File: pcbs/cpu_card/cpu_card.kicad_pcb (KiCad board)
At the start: 4 copper layers, 100 x 100 mm, 12 parts, among them J1 Conn1, J2 osc_header, U1 74LS161, Y1 ECS-2100AX-100

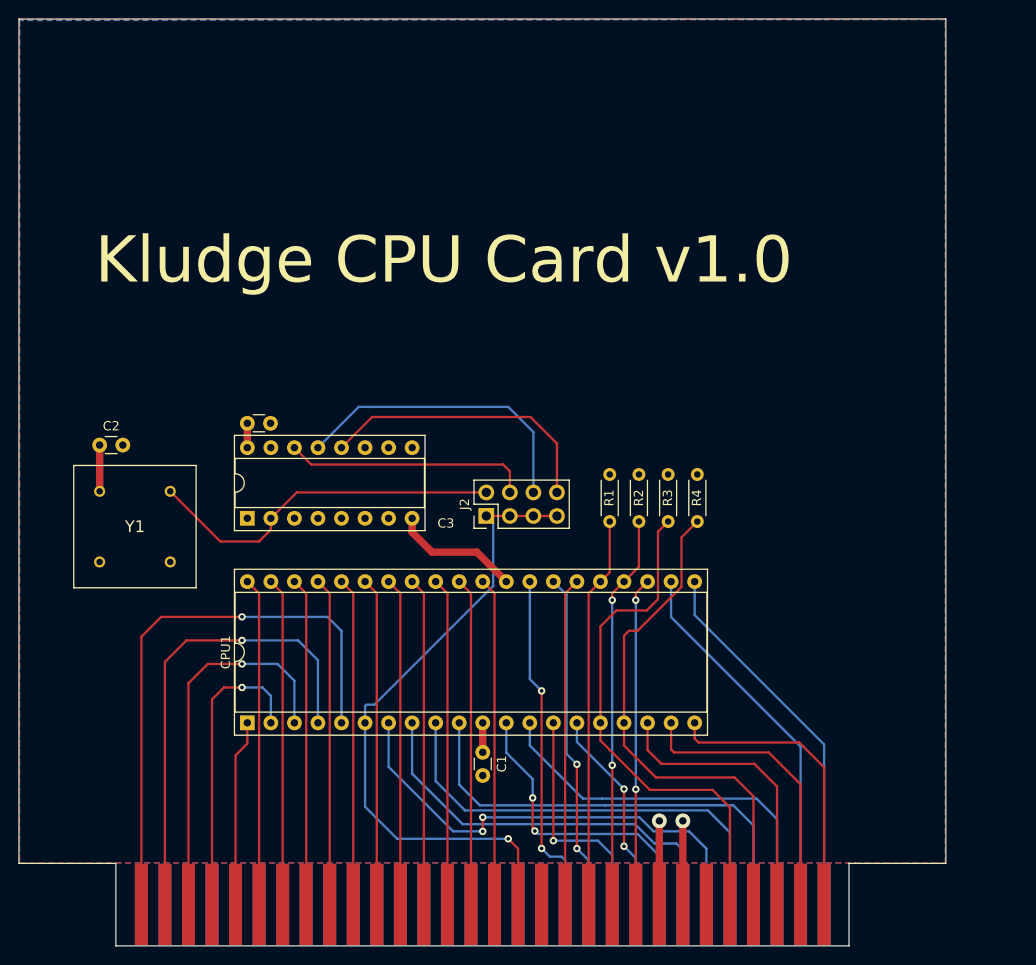
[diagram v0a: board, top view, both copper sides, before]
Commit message: changed signal traces from 0.25mm to 0.3mm and moved a few traces arround to accommodate the new size
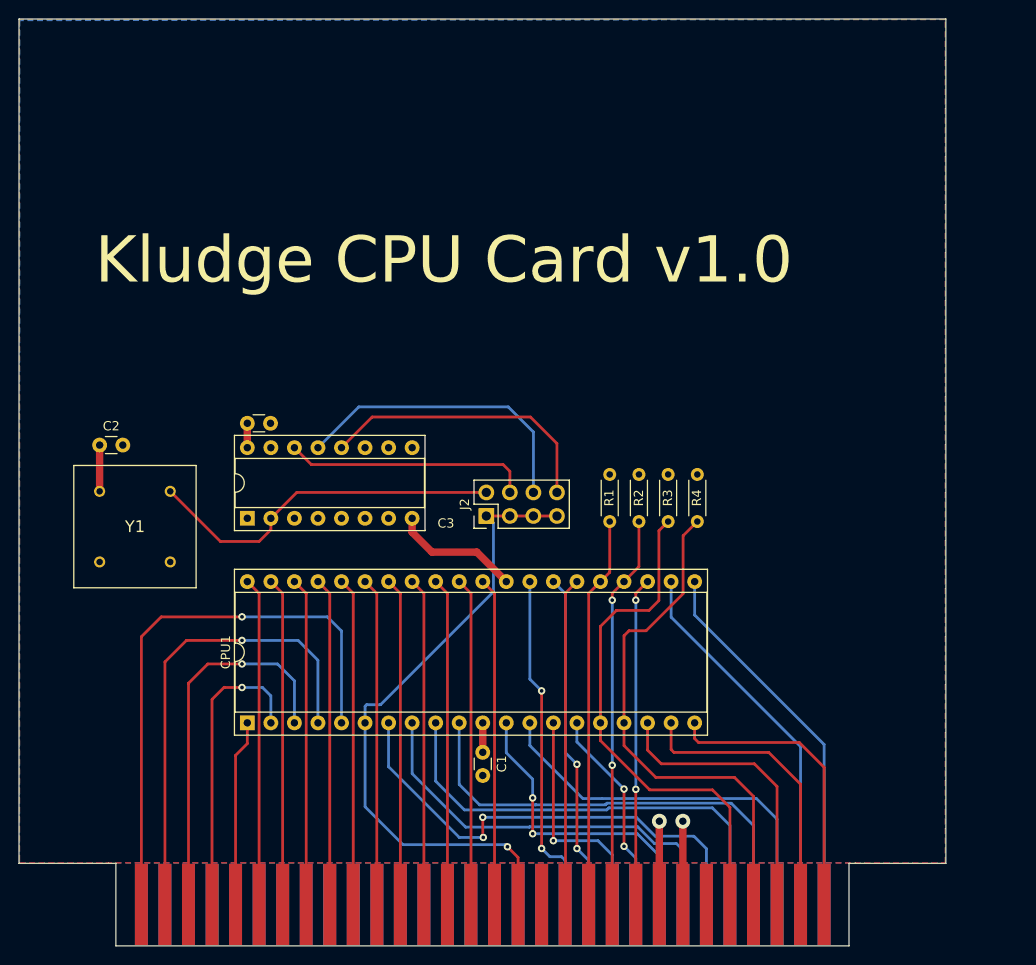
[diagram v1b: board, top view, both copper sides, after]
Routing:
- net /D4: track 50.9 -> 51.9 mm
- net /D5: track 48.1 -> 48.7 mm
- net NMI: track 55.9 -> 56.4 mm

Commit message: Changed the bus hardware to 2.54mm header and cleaned up the CPU card PCB layout
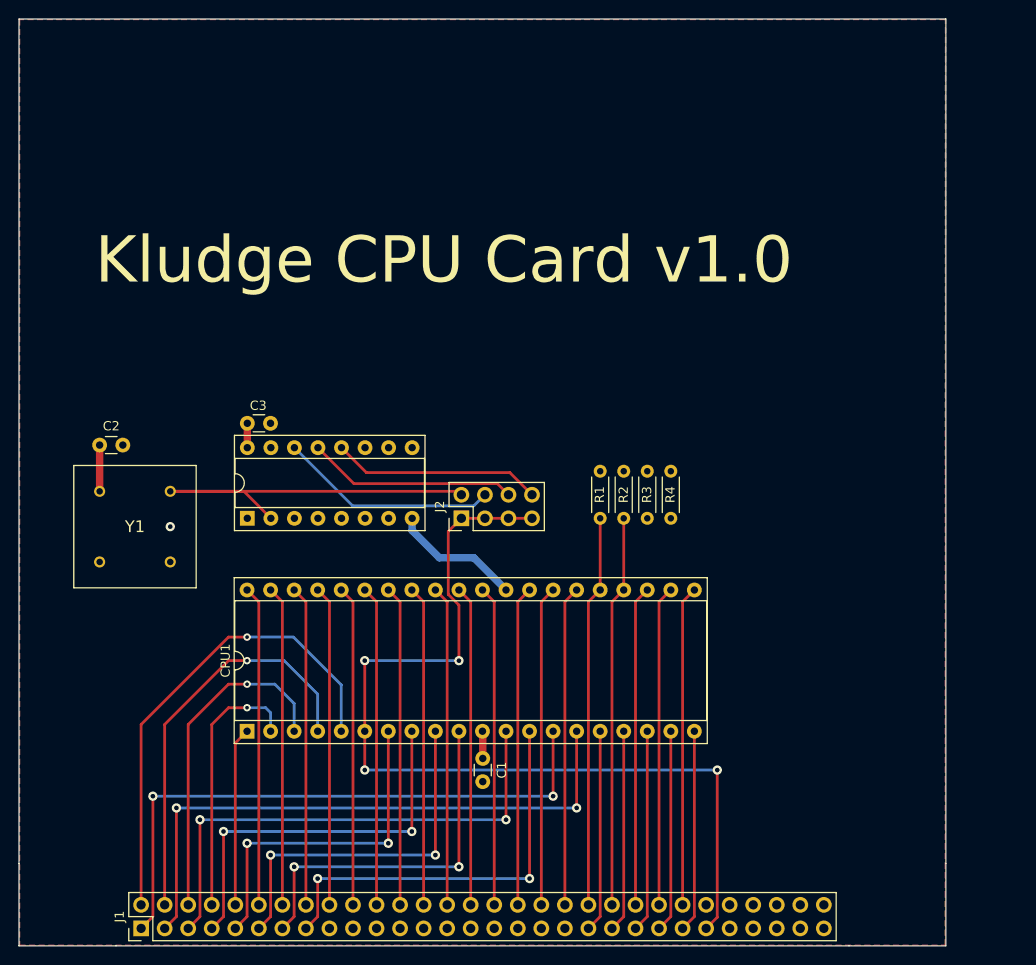
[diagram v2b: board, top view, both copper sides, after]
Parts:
- J1: footprint Z80 Parts:2x30-edge-connector -> Connector_PinHeader_2.54mm:PinHeader_2x30_P2.54mm_Vertical
- R1, R2, R3, R4: value 10K -> 3.3K
- moved J1 39.7 mm to (113.2, 148.1), turned to 90 degrees
- moved R4 2.88 mm to (170.3, 103.9)
- moved J2 2.70 mm to (147.7, 103.9)
- moved R3 2.28 mm to (167.8, 103.9)
- moved R2 1.68 mm to (165.2, 103.9)
- moved R1 1.09 mm to (162.7, 103.9)
- moved CPU1 0.91 mm to (124.6, 126.8)
- moved C1 0.66 mm to (150.0, 129.8)
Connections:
- J1 pad 1: /A15 -> /D0
- J1 pad 10: unconnected-(J1-Pin_10-Pad10) -> /A11
- J1 pad 11: /A10 -> /D5
- J1 pad 12: unconnected-(J1-Pin_12-Pad12) -> /A10
- J1 pad 13: /A9 -> /D6
- J1 pad 14: unconnected-(J1-Pin_14-Pad14) -> /A9
- J1 pad 15: /A8 -> /D7
- J1 pad 16: unconnected-(J1-Pin_16-Pad16) -> /A8
- J1 pad 17: /A7 -> unconnected-(J1-Pin_17-Pad17)
- J1 pad 18: unconnected-(J1-Pin_18-Pad18) -> /A7
- J1 pad 19: /A6 -> unconnected-(J1-Pin_19-Pad19)
- J1 pad 2: unconnected-(J1-Pin_2-Pad2) -> /A15
- J1 pad 20: unconnected-(J1-Pin_20-Pad20) -> /A6
- J1 pad 21: /A5 -> unconnected-(J1-Pin_21-Pad21)
- J1 pad 22: unconnected-(J1-Pin_22-Pad22) -> /A5
- J1 pad 23: /A4 -> unconnected-(J1-Pin_23-Pad23)
- J1 pad 24: unconnected-(J1-Pin_24-Pad24) -> /A4
- J1 pad 25: /A3 -> unconnected-(J1-Pin_25-Pad25)
- J1 pad 26: unconnected-(J1-Pin_26-Pad26) -> /A3
- J1 pad 27: /A2 -> unconnected-(J1-Pin_27-Pad27)
- J1 pad 28: unconnected-(J1-Pin_28-Pad28) -> /A2
- J1 pad 29: /A1 -> unconnected-(J1-Pin_29-Pad29)
- J1 pad 3: /A14 -> /D1
- J1 pad 30: unconnected-(J1-Pin_30-Pad30) -> /A1
- J1 pad 31: /A0 -> unconnected-(J1-Pin_31-Pad31)
- J1 pad 32: unconnected-(J1-Pin_32-Pad32) -> /A0
- J1 pad 33: SYSCLK -> GND
- J1 pad 34: unconnected-(J1-Pin_34-Pad34) -> RFSH
- J1 pad 35: unconnected-(J1-Pin_35-Pad35) -> VCC
- J1 pad 36: unconnected-(J1-Pin_36-Pad36) -> M1
- J1 pad 37: RESET -> RESET(H)
- J1 pad 38: RFSH -> RESET
- J1 pad 39: BUSRQ -> INT
- J1 pad 4: unconnected-(J1-Pin_4-Pad4) -> /A14
- J1 pad 40: M1 -> BUSRQ
- J1 pad 41: WAIT -> NMI
- J1 pad 42: /D0 -> WAIT
- J1 pad 43: BUSAK -> HALT
- J1 pad 44: /D1 -> BUSAK
- J1 pad 45: GND -> MREQ
- J1 pad 46: /D2 -> WR
- J1 pad 47: VCC -> IOREQ
- J1 pad 48: /D3 -> RD
- J1 pad 49: unconnected-(J1-Pin_49-Pad49) -> SYSCLK
- J1 pad 5: /A13 -> /D2
- J1 pad 50: /D4 -> unconnected-(J1-Pin_50-Pad50)
- J1 pad 51: INT -> unconnected-(J1-Pin_51-Pad51)
- J1 pad 52: /D5 -> unconnected-(J1-Pin_52-Pad52)
- J1 pad 53: NMI -> unconnected-(J1-Pin_53-Pad53)
- J1 pad 54: /D6 -> unconnected-(J1-Pin_54-Pad54)
- J1 pad 55: HALT -> unconnected-(J1-Pin_55-Pad55)
- J1 pad 56: /D7 -> unconnected-(J1-Pin_56-Pad56)
- J1 pad 57: MREQ -> unconnected-(J1-Pin_57-Pad57)
- J1 pad 58: WR -> unconnected-(J1-Pin_58-Pad58)
- J1 pad 59: IOREQ -> unconnected-(J1-Pin_59-Pad59)
- J1 pad 6: unconnected-(J1-Pin_6-Pad6) -> /A13
- J1 pad 60: RD -> unconnected-(J1-Pin_60-Pad60)
- J1 pad 7: /A12 -> /D3
- J1 pad 8: unconnected-(J1-Pin_8-Pad8) -> /A12
- J1 pad 9: /A11 -> /D4
- U1 pad 3: unconnected-(U1-D0-Pad3) -> GND
- U1 pad 4: unconnected-(U1-D1-Pad4) -> GND
- U1 pad 5: unconnected-(U1-D2-Pad5) -> GND
- U1 pad 6: unconnected-(U1-D3-Pad6) -> GND
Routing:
- net /D1: track 22.2 -> 65.0 mm
- net /D0: track 25.1 -> 65.0 mm, vias 1 -> 2
- net NMI: track 56.4 -> 21.8 mm
- net INT: track 56.2 -> 21.8 mm
- net SYSCLK: track 69.8 -> 101.6 mm, vias 1 -> 4
- net /D2: track 33.1 -> 54.8 mm
- net /D4: track 51.9 -> 37.0 mm
- net /1/4: track 32.7 -> 22.7 mm
- net IOREQ: track 31.8 -> 21.8 mm
- net /A15: track 61.9 -> 52.1 mm
- net MREQ: track 31.4 -> 21.8 mm
- net HALT: track 31.3 -> 21.8 mm
- net /D6: track 48.9 -> 39.6 mm, vias 0 -> 2
- net VCC: track 19.8 -> 10.6 mm, vias 1 -> 0
- net /D5: track 48.7 -> 39.6 mm, vias 0 -> 2
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- added copper zone on In1.Cu, net GND
- added copper zone on In2.Cu, net VCC
- removed copper zone on In2.Cu, net GND
- removed copper zone on In1.Cu, net VCC
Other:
- outline, holes or cut-outs redrawn

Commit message: Changed CPU board to nominal 20MHz with the option to adjust using the 2x5 header.
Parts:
- J2: footprint Connector_PinHeader_2.54mm:PinHeader_2x04_P2.54mm_Vertical -> Connector_PinHeader_2.54mm:PinHeader_2x05_P2.54mm_Vertical
- Y1: value ECS-2100AX-100 -> ECS-2100AX-200; footprint Z80 Parts:ECS-2100AX-100 -> Z80 Parts:ECS-2100AX-200
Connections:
- net /1/2 renamed /10 MHz
- net /1/4 renamed /5 MHz
- net /1/8 renamed /2.5 MHz
- U1 pad 11: unconnected-(U1-Q3-Pad11) -> /1.25 MHz
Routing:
- net NMI: track 21.8 -> 46.9 mm
- net INT: track 21.8 -> 46.9 mm
- net /1.25 MHz: track 0.00 -> 22.7 mm
- net SYSCLK: track 101.6 -> 104.2 mm

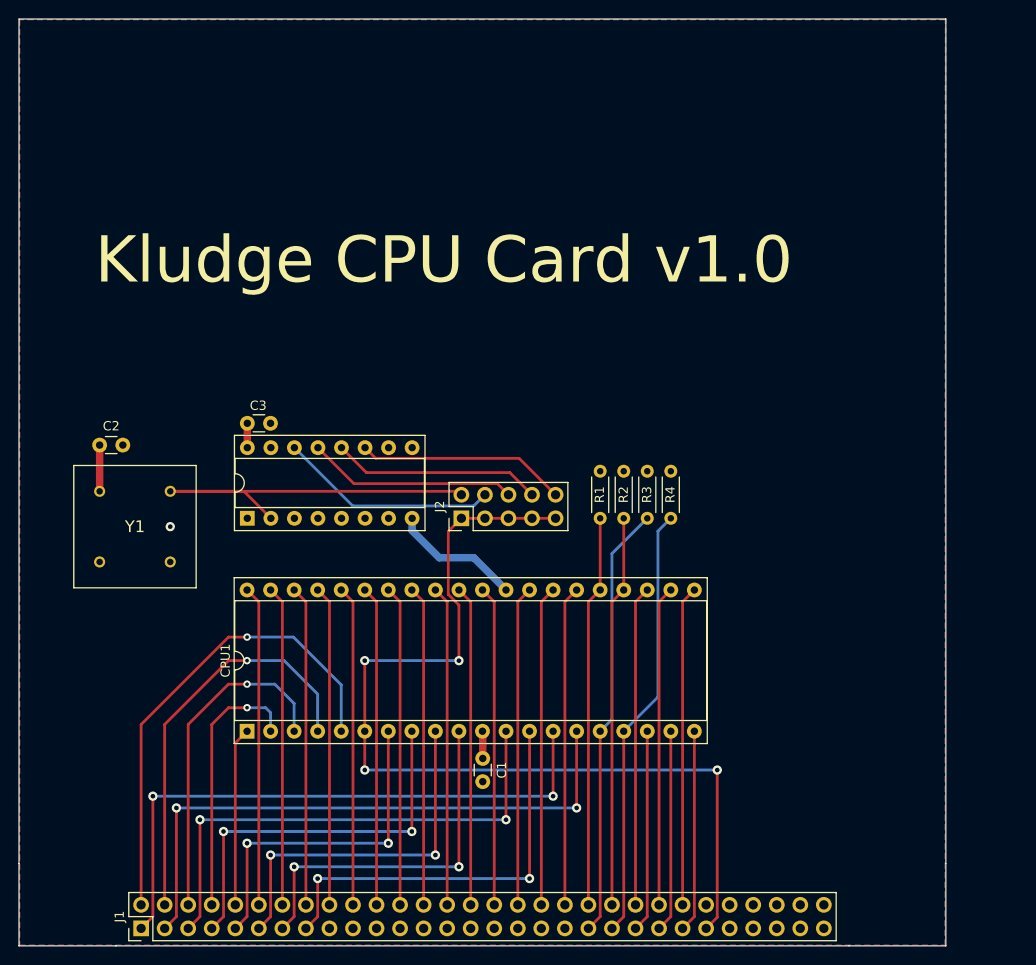
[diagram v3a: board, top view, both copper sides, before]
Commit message: Mostly finished with cpu_card, added early prototypes of backplane and protoboard cards. Also added the libraries used for this project
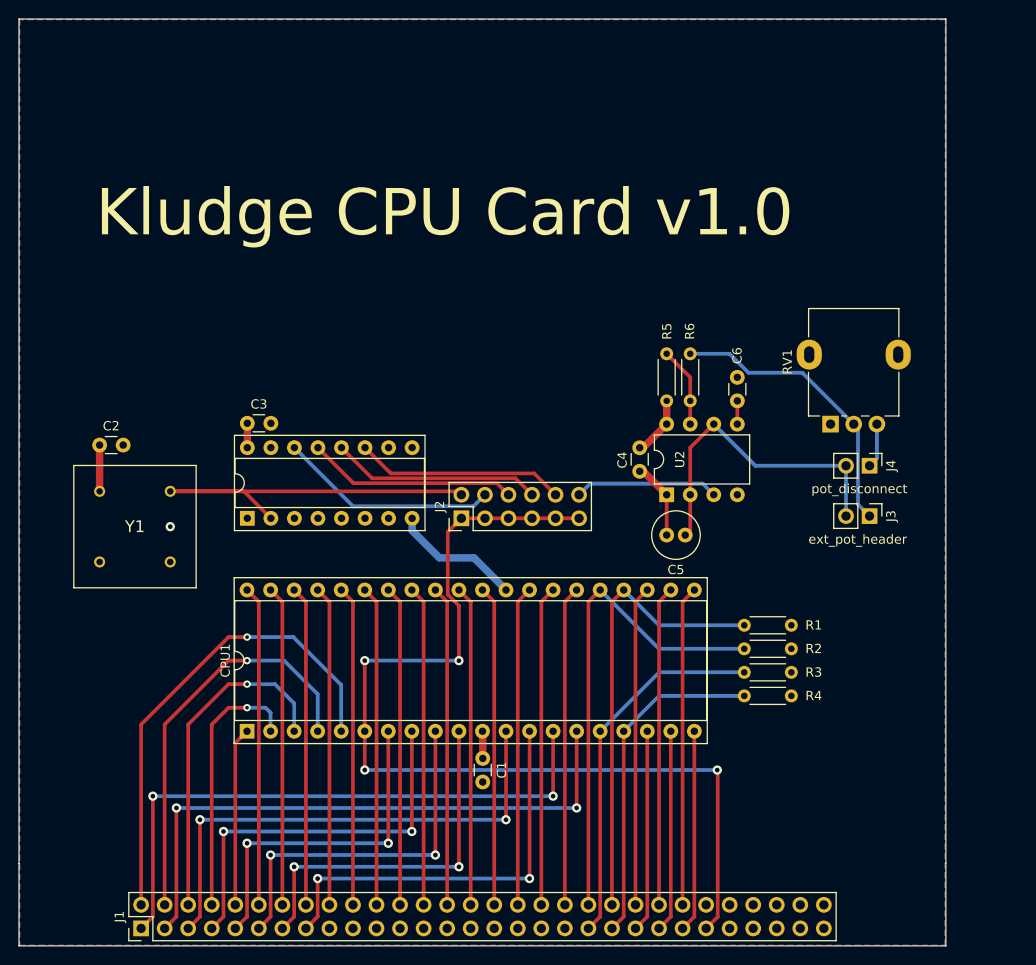
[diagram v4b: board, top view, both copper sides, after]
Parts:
- added C4: 100 nF, Z80 Parts:C_Disc_D3.0mm_W1.6mm_P2.54mm, F.Cu at (167.0, 96.3)
- added C5: 1 uF, Capacitor_THT:C_Radial_D5.0mm_H11.0mm_P2.00mm, F.Cu at (171.9, 105.7)
- added C6: 0.01 uF, Z80 Parts:C_Disc_D3.0mm_W1.6mm_P2.54mm, F.Cu at (177.5, 91.2)
- added J3: ext_pot_header, Connector_PinHeader_2.54mm:PinHeader_1x02_P2.54mm_Vertical, F.Cu at (191.8, 103.6)
- added J4: pot_disconnect, Connector_PinHeader_2.54mm:PinHeader_1x02_P2.54mm_Vertical, F.Cu at (191.8, 98.2)
- added R5: 1K, Resistor_THT:R_Axial_DIN0204_L3.6mm_D1.6mm_P5.08mm_Horizontal, F.Cu at (169.9, 91.2)
- added R6: 1K, Resistor_THT:R_Axial_DIN0204_L3.6mm_D1.6mm_P5.08mm_Horizontal, F.Cu at (172.4, 91.2)
- added RV1: 1M, Potentiometer_THT:Potentiometer_Alpha_RD901F-40-00D_Single_Vertical, F.Cu at (187.6, 93.7)
- added U2: ICM7555xP, Package_DIP:DIP-8_W7.62mm, F.Cu at (169.9, 101.3)
- C1, C2, C3: footprint Capacitor_THT:C_Disc_D3.0mm_W1.6mm_P2.50mm -> Z80 Parts:C_Disc_D3.0mm_W1.6mm_P2.54mm
- J2: footprint Connector_PinHeader_2.54mm:PinHeader_2x05_P2.54mm_Vertical -> Connector_PinHeader_2.54mm:PinHeader_2x06_P2.54mm_Vertical
- moved R4 20.7 mm to (178.2, 123.0), turned to 0 degrees
- moved R3 19.6 mm to (178.2, 120.5), turned to 0 degrees
- moved R1 19.4 mm to (178.2, 115.4), turned to 0 degrees
- moved R2 19.2 mm to (178.2, 118.0), turned to 0 degrees
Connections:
- R1 pad 1: BUSRQ -> WAIT
- R2 pad 1: WAIT -> BUSRQ
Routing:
- net Net-(J3-Pin_2): track 0.00 -> 34.8 mm
- net Net-(J3-Pin_1): track 0.00 -> 31.4 mm
- net OSC_ADJ: track 0.00 -> 15.5 mm
- net NMI: track 46.9 -> 36.4 mm
- net BUSRQ: track 42.2 -> 52.7 mm
- net Net-(U2-DIS): track 0.00 -> 8.64 mm
- net GND: track 14.1 -> 22.4 mm
- net INT: track 46.9 -> 40.0 mm
- net WAIT: track 42.2 -> 49.1 mm
- net VCC: track 10.6 -> 17.0 mm
- net Net-(J4-Pin_1): track 0.00 -> 4.82 mm
- net SYSCLK: track 104.2 -> 106.8 mm
- net Net-(U2-CV): track 0.00 -> 2.51 mm
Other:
- outline, holes or cut-outs redrawn
- board text removed: "C3"
